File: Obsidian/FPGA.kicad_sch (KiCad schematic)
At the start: 45 parts, among them Q1 BSS138LT1G, Q2 BSS138LT1G, SW2 SW_DIP_x01, U1 XC7A35T-CSG325, U28 24AA256UID-I_ST

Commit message: update LCSC reference, and OFFSET rotation for JLCPCB
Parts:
- LD3, LD4: LCSC C5879295 -> C598257
- U28: FT Rotation Offset (none) -> 270
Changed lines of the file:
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@@
 			)
 		)
-		(property "LCSC" "C5879295"
+		(property "LCSC" "C598257"
 			(at 179.07 240.03 90)
 			(effects
@@
 			)
 		)
-		(property "FT Rotation Offset" ""
+		(property "FT Rotation Offset" "270"
 			(at 106.68 232.41 0)
 			(effects
@@
 			)
 		)
-		(property "LCSC" "C5879295"
+		(property "LCSC" "C598257"
 			(at 214.63 240.03 90)
 			(effects

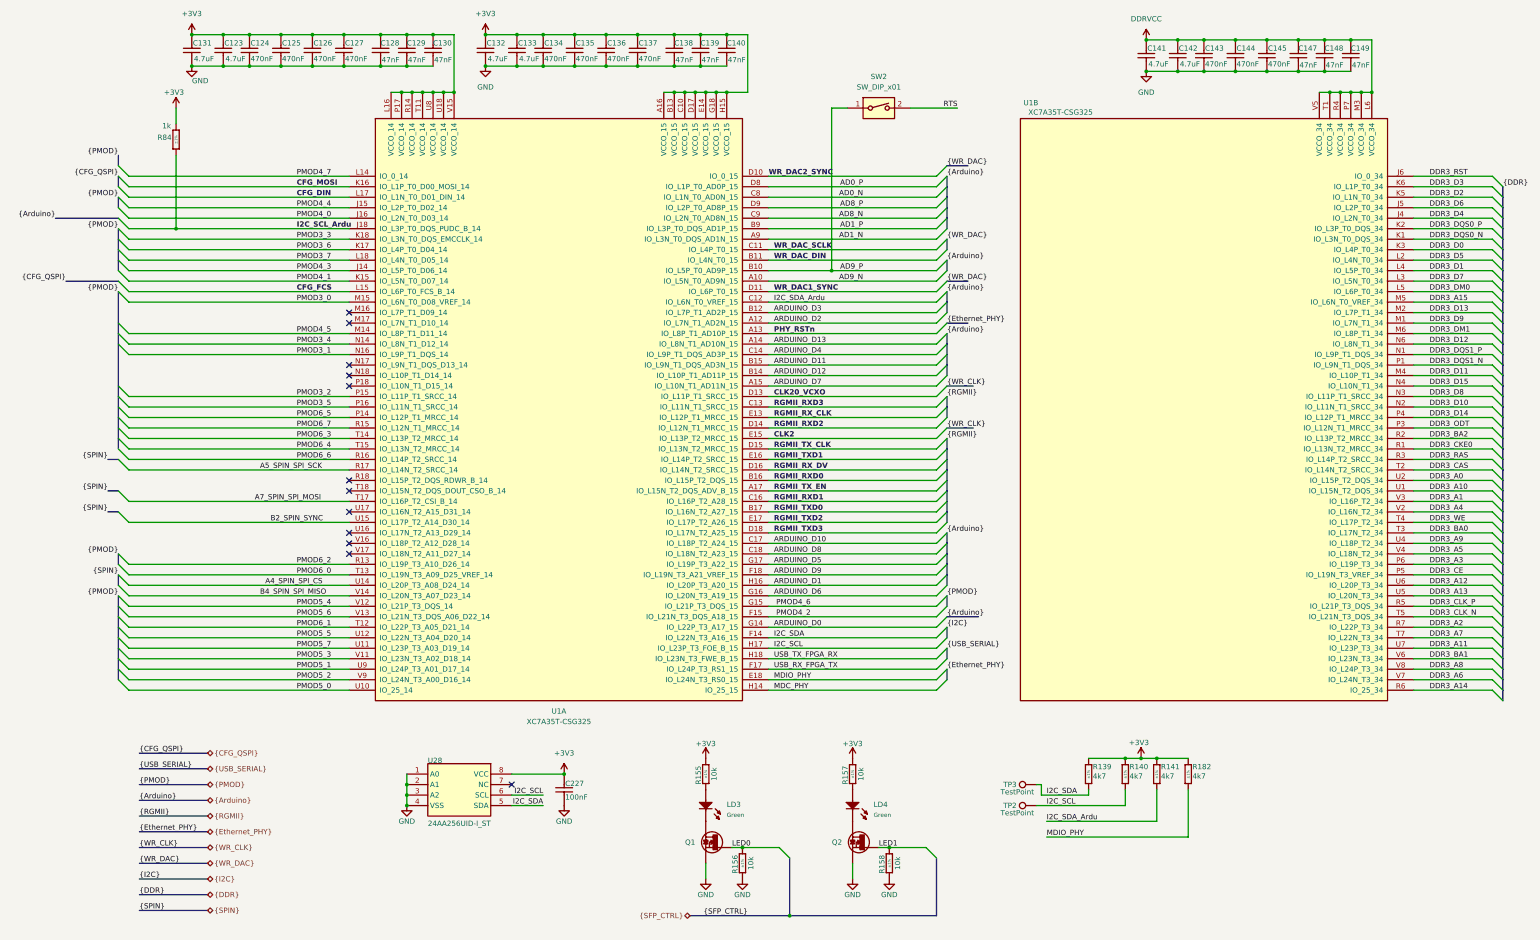
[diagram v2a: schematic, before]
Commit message: Cleaning symbol fields
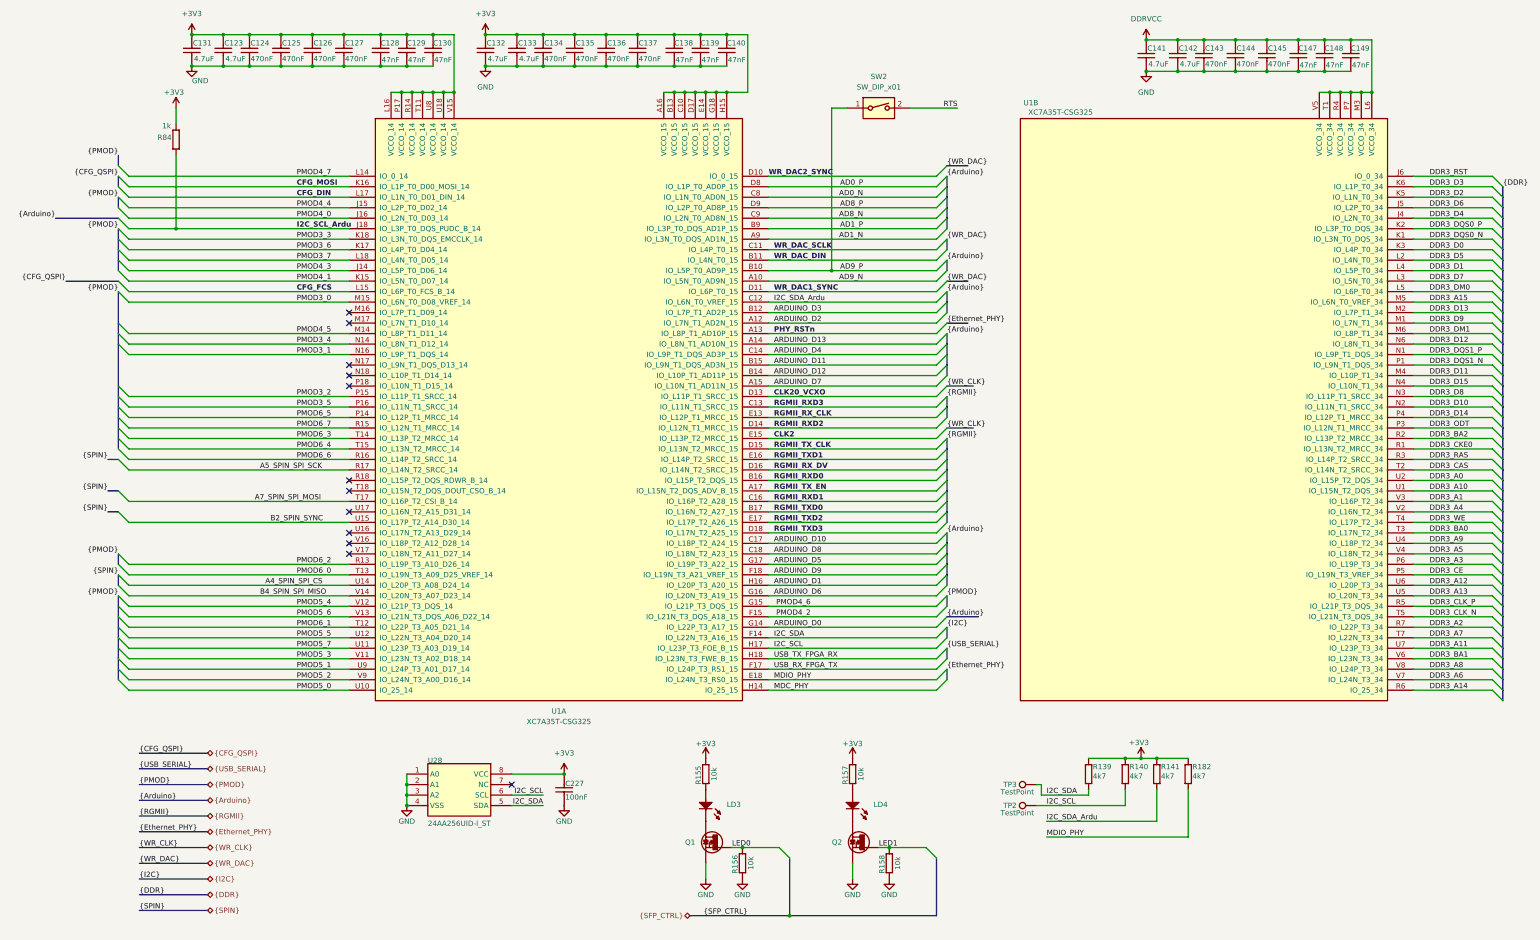
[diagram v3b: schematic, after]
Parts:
- C123, C131, C132, C133, C141, C142: Author CERN DEM BC -> (none); Case 0402 -> (none); Comment 4.7uF -> (none); Component Kind Standard -> (none); Component Type Standard -> (none); ComponentHeight (none) -> (none); CreateDate 09/07/20 00:00:00 -> (none); Database Table Name Capacitors -> (none); Footprint Library Capacitors SMD -> (none); Footprint Path PcbLib\Capacitors SMD.PcbLib -> (none); Footprint Ref CAPC1005X55N -> (none); HelpURL \\cern.ch\dfs\Applications\Altium\Datasheets\CC0402_X5R_YAG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 -> (none); LatestRevisionDate 09/07/20 00:00:00 -> (none); Library Name Capacitors SMD -> (none); Library Path SchLib\Capacitors.SchLib -> (none); Library Ref Capacitor - non polarized -> (none); License CC-BY-SA 4.0 -> (none); Manufacturer GENERIC -> (none); Manufacturer Part Number CC0402_4.7UF_16V_20%_X5R -> (none); Manufacturer1 ComponentHeight 0.55mm -> (none); Manufacturer1 Example YAGEO PHYCOMP -> (none); Manufacturer1 Part Number CC0402MRX5R7BB475 -> (none); Mounted Yes -> (none); PackageDescription (none) -> (none); Part Description SMD Multilayer Chip Ceramic Capacitor -> (none); Part Number CC0402_4.7UF_16V_20%_X5R -> (none); Pin Count 2 -> (none); PressFit (none) -> (none); SMD Yes -> (none); Sense No -> (none); Sense Comment (none) -> (none); Socket No -> (none); Status Preferred -> (none); Status Comment (none) -> (none); TC X5R -> (none); Tolerance ±20% -> (none); Voltage 16V -> (none)
- C124, C125, C126, C127, C134, C135, C136, C137, C143, C144, C145: Author CERN DEM JLC -> (none); Case 0201 -> (none); Comment 470nF -> (none); Component Kind Standard -> (none); Component Type Standard -> (none); ComponentHeight (none) -> (none); CreateDate 05/27/10 00:00:00 -> (none); Database Table Name Capacitors -> (none); Footprint Library Capacitors SMD -> (none); Footprint Path PcbLib\Capacitors SMD.PcbLib -> (none); Footprint Ref CAPC0603X33N -> (none); HelpURL \\cern.ch\dfs\Applications\Altium\Datasheets\CC0201_X5R_TAI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 -> (none); LatestRevisionDate 05/27/10 00:00:00 -> (none); Library Name Capacitors SMD -> (none); Library Path SchLib\Capacitors.SchLib -> (none); Library Ref Capacitor - non polarized -> (none); License CC-BY-SA 4.0 -> (none); Manufacturer GENERIC -> (none); Manufacturer Part Number CC0201_470NF_4V_20%_X5R -> (none); Manufacturer1 ComponentHeight 0.33mm -> (none); Manufacturer1 Example TAIYO YUDEN -> (none); Manufacturer1 Part Number AMK063BJ474MP-F -> (none); Mounted Yes -> (none); PackageDescription (none) -> (none); Part Description SMD Multilayer Chip Ceramic Capacitor -> (none); Part Number CC0201_470NF_4V_20%_X5R -> (none); Pin Count 2 -> (none); PressFit (none) -> (none); SMD Yes -> (none); Sense No -> (none); Sense Comment (none) -> (none); Socket No -> (none); Status Not Recommended -> (none); Status Comment (none) -> (none); TC X5R -> (none); Tolerance ±20% -> (none); Voltage 4V -> (none)
- C128, C129, C130, C138, C139, C140, C147, C148, C149: Author CERN DEM JLC -> (none); Case 0201 -> (none); Comment 47nF -> (none); Component Kind Standard -> (none); Component Type Standard -> (none); ComponentHeight (none) -> (none); CreateDate 12/03/07 00:00:00 -> (none); Database Table Name Capacitors -> (none); Footprint Library Capacitors SMD -> (none); Footprint Path PcbLib\Capacitors SMD.PcbLib -> (none); Footprint Ref CAPC0603X33N -> (none); HelpURL \\cern.ch\dfs\Applications\Altium\Datasheets\CC0201_X5R_AVX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 -> (none); LatestRevisionDate 12/03/07 00:00:00 -> (none); Library Name Capacitors SMD -> (none); Library Path SchLib\Capacitors.SchLib -> (none); Library Ref Capacitor - non polarized -> (none); License CC-BY-SA 4.0 -> (none); Manufacturer GENERIC -> (none); Manufacturer Part Number CC0201_47NF_6.3V_10%_X5R -> (none); Manufacturer1 ComponentHeight 0.33mm -> (none); Manufacturer1 Example AVX -> (none); Manufacturer1 Part Number 02016D473KAT2A -> (none); Mounted Yes -> (none); PackageDescription (none) -> (none); Part Description SMD Multilayer Chip Ceramic Capacitor -> (none); Part Number CC0201_47NF_6.3V_10%_X5R -> (none); Pin Count 2 -> (none); PressFit (none) -> (none); SMD Yes -> (none); Sense No -> (none); Sense Comment (none) -> (none); Socket No -> (none); Status Not Recommended -> (none); Status Comment (none) -> (none); TC X5R -> (none); Tolerance ±10% -> (none); Voltage 6.3V -> (none)
- C227: Author CERN DEM MR -> (none); Case 0402 -> (none); Comment 100nF -> (none); Component Kind Standard -> (none); Component Type Standard -> (none); ComponentHeight (none) -> (none); CreateDate 06/30/17 00:00:00 -> (none); Database Table Name Capacitors -> (none); Footprint Library Capacitors SMD -> (none); Footprint Path PcbLib\Capacitors SMD.PcbLib -> (none); Footprint Ref CAPC1005X55N -> (none); HelpURL \\cern.ch\dfs\Applications\Altium\Datasheets\CC0402_MURATA_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 -> (none); LatestRevisionDate 06/30/17 00:00:00 -> (none); Library Name Capacitors SMD -> (none); Library Path SchLib\Capacitors.SchLib -> (none); Library Ref Capacitor - non polarized -> (none); License CC-BY-SA 4.0 -> (none); Manufacturer GENERIC -> (none); Manufacturer Part Number CC0402_100NF_50V_10%_X7R -> (none); Manufacturer1 ComponentHeight 0.55mm -> (none); Manufacturer1 Example MURATA -> (none); Manufacturer1 Part Number GRM155R71H104KE14D -> (none); Mounted Yes -> (none); PackageDescription (none) -> (none); Part Description SMD Multilayer Chip Ceramic Capacitor -> (none); Part Number CC0402_100NF_50V_10%_X7R -> (none); Pin Count 2 -> (none); PressFit (none) -> (none); SMD Yes -> (none); Sense No -> (none); Sense Comment (none) -> (none); Socket No -> (none); Status None -> (none); Status Comment (none) -> (none); TC X7R -> (none); Tolerance ±10% -> (none); Voltage 50V -> (none)
- LD3, LD4: Author CERN DEM JLC -> (none); Bonding No -> (none); Case 0603 -> (none); Color Green -> (none); Comment (none) -> (none); Component Kind Standard -> (none); Component Type Standard -> (none); ComponentHeight 0.65mm -> (none); ComponentLink1Description (none) -> (none); ComponentLink1URL (none) -> (none); ComponentLink2Description (none) -> (none); ComponentLink2URL (none) -> (none); CreateDate 07/03/17 00:00:00 -> (none); Database Table Name ICs And Semiconductors -> (none); Device (none) -> (none); Footprint Library ICs And Semiconductors SMD -> (none); Footprint Path PcbLib\ICs And Semiconductors SMD.PcbLib -> (none); Footprint Ref LED_KINGBRIGHT_KPH-1608CGCK -> (none); HelpURL \\cern.ch\dfs\Applications\Altium\Datasheets\LED_KINGBRIGHT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 -> (none); LatestRevisionDate 07/03/17 00:00:00 -> (none); Library Name LEDs & Displays -> (none); Library Path SchLib\LEDs & Displays.SchLib -> (none); Library Ref LED Green 1C 2A -> (none); License CC-BY-SA 4.0 -> (none); Manufacturer KINGBRIGHT -> (none); Manufacturer Part Number KPH-1608CGCK -> (none); Mounted Yes -> (none); PackageDescription SMT Green LED, Case 0603, Body L 1.6 x W 0.8mm H 0.65mm -> (none); Part Description SMD Green LED, Case 1.6mmX0.8mm(0603), 0.65mm Thickness -> (none); Part Number LED_KINGBRIGHT_KPH-1608CGCK -> (none); Pin Count 2 -> (none); PressFit No -> (none); SMD Yes -> (none); Sense No -> (none); Sense Comment (none) -> (none); Socket No -> (none); Status (none) -> (none); Status Comment (none) -> (none)
- Q1, Q2: Author CERN DEM JLC -> (none); Bonding No -> (none); Case SOT23-3 -> (none); Comment BSS138LT1G -> (none); Component Kind Standard -> (none); Component Type Standard -> (none); ComponentHeight 1.11mm -> (none); ComponentLink1Description (none) -> (none); ComponentLink1URL (none) -> (none); ComponentLink2Description (none) -> (none); ComponentLink2URL (none) -> (none); CreateDate 03/23/09 00:00:00 -> (none); Database Table Name ICs And Semiconductors -> (none); Device BSS138LT1G -> (none); Footprint Library ICs And Semiconductors SMD -> (none); Footprint Path PcbLib\ICs And Semiconductors SMD.PcbLib -> (none); Footprint Ref SOT95P240X110-3N -> (none); HelpURL \\cern.ch\dfs\Applications\Altium\Datasheets\BSS138LT1G.pdf -> (none); LatestRevisionDate 05/25/22 00:00:00 -> (none); LatestRevisionDate1 (none) -> (none); Library Name Transistors -> (none); Library Path SchLib\Transistors.SchLib -> (none); Library Ref N-MOSFET-D 1G 2S 3D -> (none); License CC-BY-SA 4.0 -> (none); Manufacturer ON SEMICONDUCTOR -> (none); Manufacturer Part Number BSS138L -> (none); Mounted Yes -> (none); PackageDescription SOT23, 0.95mm Pitch; 3 Pin, 1.40mm W X 3.00mm L X 1.10mm H 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 -> (none); Part Description 50V, 200mA N-Channel Enhancement Mode Field-Effect Transist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 -> (none); Part Number BSS138LT1G -> (none); Pin Count 3 -> (none); PressFit No -> (none); SCEM (none) -> (none); SMD Yes -> (none); Sense No -> (none); Sense Comment (none) -> (none); Socket No -> (none); Status (none) -> (none); Status Comment (none) -> (none)
- R139, R140, R141, R182: Author CERN DEM JLC -> (none); Case 0402 -> (none); Comment 4k7 -> (none); Component Kind Standard -> (none); Component Type Standard -> (none); ComponentHeight (none) -> (none); CreateDate 12/03/07 00:00:00 -> (none); Database Table Name Resistors -> (none); Footprint Library Resistors SMD -> (none); Footprint Path PcbLib\Resistors SMD.PcbLib -> (none); Footprint Ref RESC1005X40N -> (none); HelpURL \\cern.ch\dfs\Applications\Altium\Datasheets\R0402_Phycomp_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 -> (none); LatestRevisionDate 10/17/12 00:00:00 -> (none); Library Name Resistors SMD -> (none); Library Path SchLib\Resistors.SchLib -> (none); Library Ref Resistor - 1% -> (none); License CC-BY-SA 4.0 -> (none); Manufacturer GENERIC -> (none); Manufacturer Part Number R0402_4K7_1%_0.0625W_100PPM -> (none); Manufacturer1 ComponentHeight 0.4mm -> (none); Manufacturer1 Example YAGEO PHYCOMP -> (none); Manufacturer1 Part Number 232270674702L -> (none); Mounted Yes -> (none); PackageDescription (none) -> (none); Part Description General Purpose Thick Film Chip Resistor -> (none); Part Number R0402_4K7_1%_0.0625W_100PPM -> (none); Pin Count 2 -> (none); Power 0.0625W -> (none); PressFit No -> (none); SMD Yes -> (none); Sense No -> (none); Sense Comment (none) -> (none); Socket No -> (none); Status Not Recommended -> (none); Status Comment (none) -> (none); TC ±100ppm/°C -> (none); Tolerance ±1% -> (none); Voltage (none) -> (none)
- R155, R156, R157, R158: Author CERN DEM JLC -> (none); Case 0402 -> (none); Comment 10k -> (none); Component Kind Standard -> (none); Component Type Standard -> (none); ComponentHeight (none) -> (none); CreateDate 12/03/07 00:00:00 -> (none); Database Table Name Resistors -> (none); Footprint Library Resistors SMD -> (none); Footprint Path PcbLib\Resistors SMD.PcbLib -> (none); Footprint Ref RESC1005X40N -> (none); HelpURL \\cern.ch\dfs\Applications\Altium\Datasheets\R0402_Phycomp_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 -> (none); LatestRevisionDate 10/17/12 00:00:00 -> (none); Library Name Resistors SMD -> (none); Library Path SchLib\Resistors.SchLib -> (none); Library Ref Resistor - 1% -> (none); License CC-BY-SA 4.0 -> (none); Manufacturer GENERIC -> (none); Manufacturer Part Number R0402_10K_1%_0.0625W_100PPM -> (none); Manufacturer1 ComponentHeight 0.4mm -> (none); Manufacturer1 Example YAGEO PHYCOMP -> (none); Manufacturer1 Part Number 232270671003L -> (none); Mounted Yes -> (none); PackageDescription (none) -> (none); Part Description General Purpose Thick Film Chip Resistor -> (none); Part Number R0402_10K_1%_0.0625W_100PPM -> (none); Pin Count 2 -> (none); Power 0.0625W -> (none); PressFit No -> (none); SMD Yes -> (none); Sense No -> (none); Sense Comment (none) -> (none); Socket No -> (none); Status Not Recommended -> (none); Status Comment (none) -> (none); TC ±100ppm/°C -> (none); Tolerance ±1% -> (none); Voltage (none) -> (none)
- R84: Author CERN DEM JLC -> (none); Case 0402 -> (none); Comment 1k -> (none); Component Kind Standard -> (none); Component Type Standard -> (none); ComponentHeight (none) -> (none); CreateDate 12/03/07 00:00:00 -> (none); Database Table Name Resistors -> (none); Footprint Library Resistors SMD -> (none); Footprint Path PcbLib\Resistors SMD.PcbLib -> (none); Footprint Ref RESC1005X40N -> (none); HelpURL \\cern.ch\dfs\Applications\Altium\Datasheets\R0402_Phycomp_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 -> (none); LatestRevisionDate 10/17/12 00:00:00 -> (none); Library Name Resistors SMD -> (none); Library Path SchLib\Resistors.SchLib -> (none); Library Ref Resistor - 1% -> (none); License CC-BY-SA 4.0 -> (none); Manufacturer GENERIC -> (none); Manufacturer Part Number R0402_1K_1%_0.0625W_100PPM -> (none); Manufacturer1 ComponentHeight 0.4mm -> (none); Manufacturer1 Example YAGEO PHYCOMP -> (none); Manufacturer1 Part Number 232270671002L -> (none); Mounted Yes -> (none); PackageDescription (none) -> (none); Part Description General Purpose Thick Film Chip Resistor -> (none); Part Number R0402_1K_1%_0.0625W_100PPM -> (none); Pin Count 2 -> (none); Power 0.0625W -> (none); PressFit No -> (none); SMD Yes -> (none); Sense No -> (none); Sense Comment (none) -> (none); Socket No -> (none); Status Not Recommended -> (none); Status Comment (none) -> (none); TC ±100ppm/°C -> (none); Tolerance ±1% -> (none); Voltage (none) -> (none)
- U28: ARROW PART NUMBER 24AA256UID-I/ST -> (none); ARROW PRICE/STOCK https://www.arrow.com/en/products/24aa256uid-ist/microchip-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 -> (none); DATASHEET LINK https://datasheet.datasheetarchive.com/originals/distributo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 -> (none); GEOMETRY.HEIGHT 1.2mm -> (none); MANUFACTURER_NAME Microchip -> (none); MANUFACTURER_PART_NUMBER 24AA256UID-I/ST -> (none); MOUSER PART NUMBER 579-24AA256UID-I/ST -> (none); MOUSER PRICE/STOCK https://www.mouser.co.uk/ProductDetail/Microchip-Technology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 -> (none)

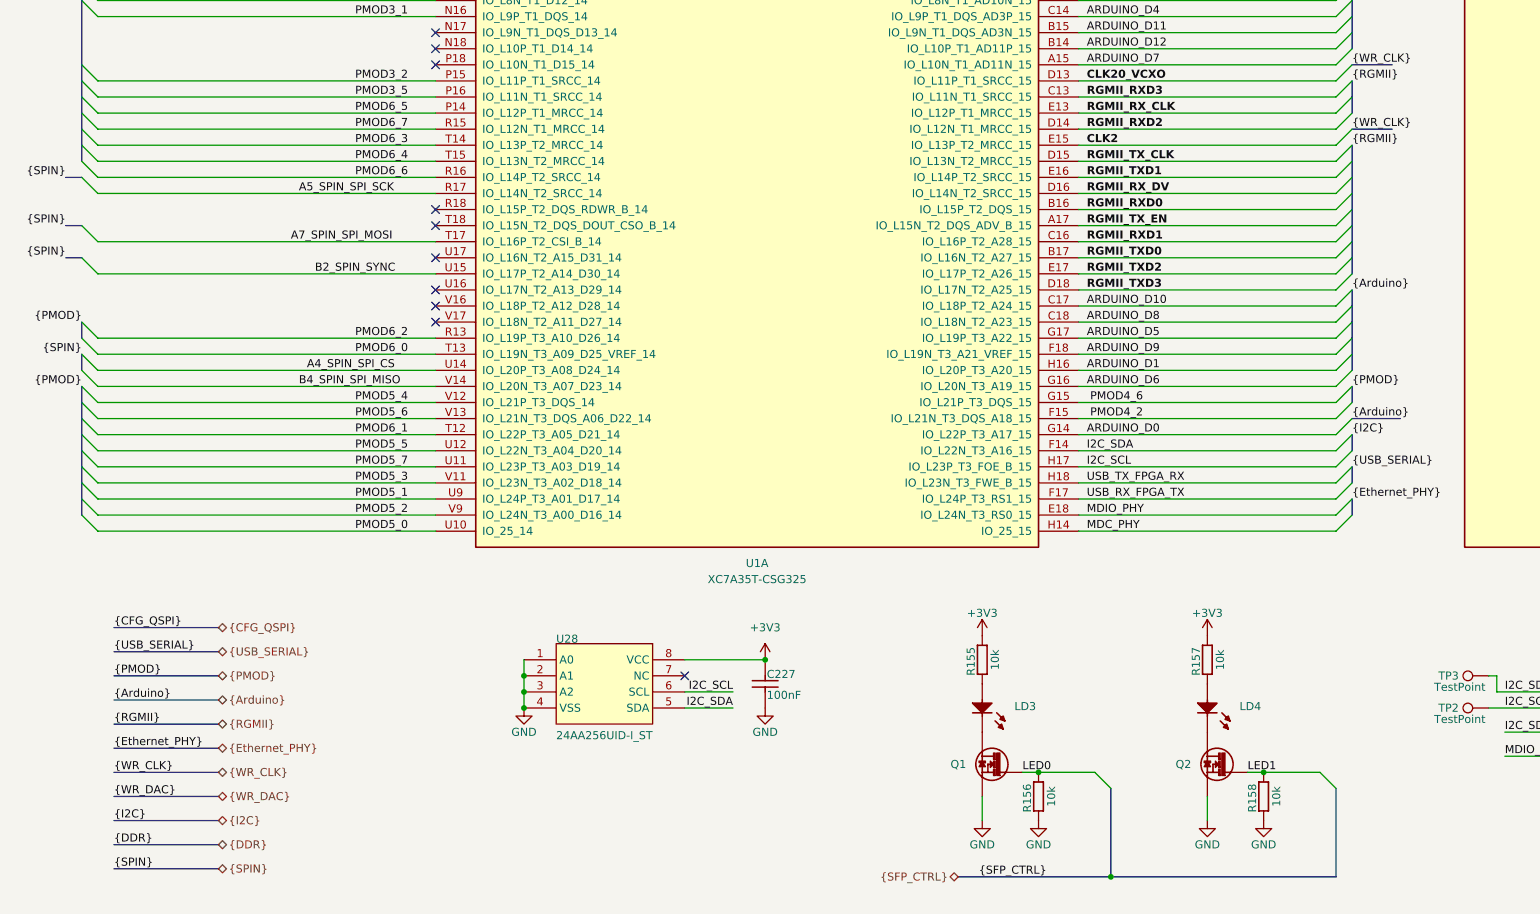
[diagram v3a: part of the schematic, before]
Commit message: Separating auxiliary clock from WR clock
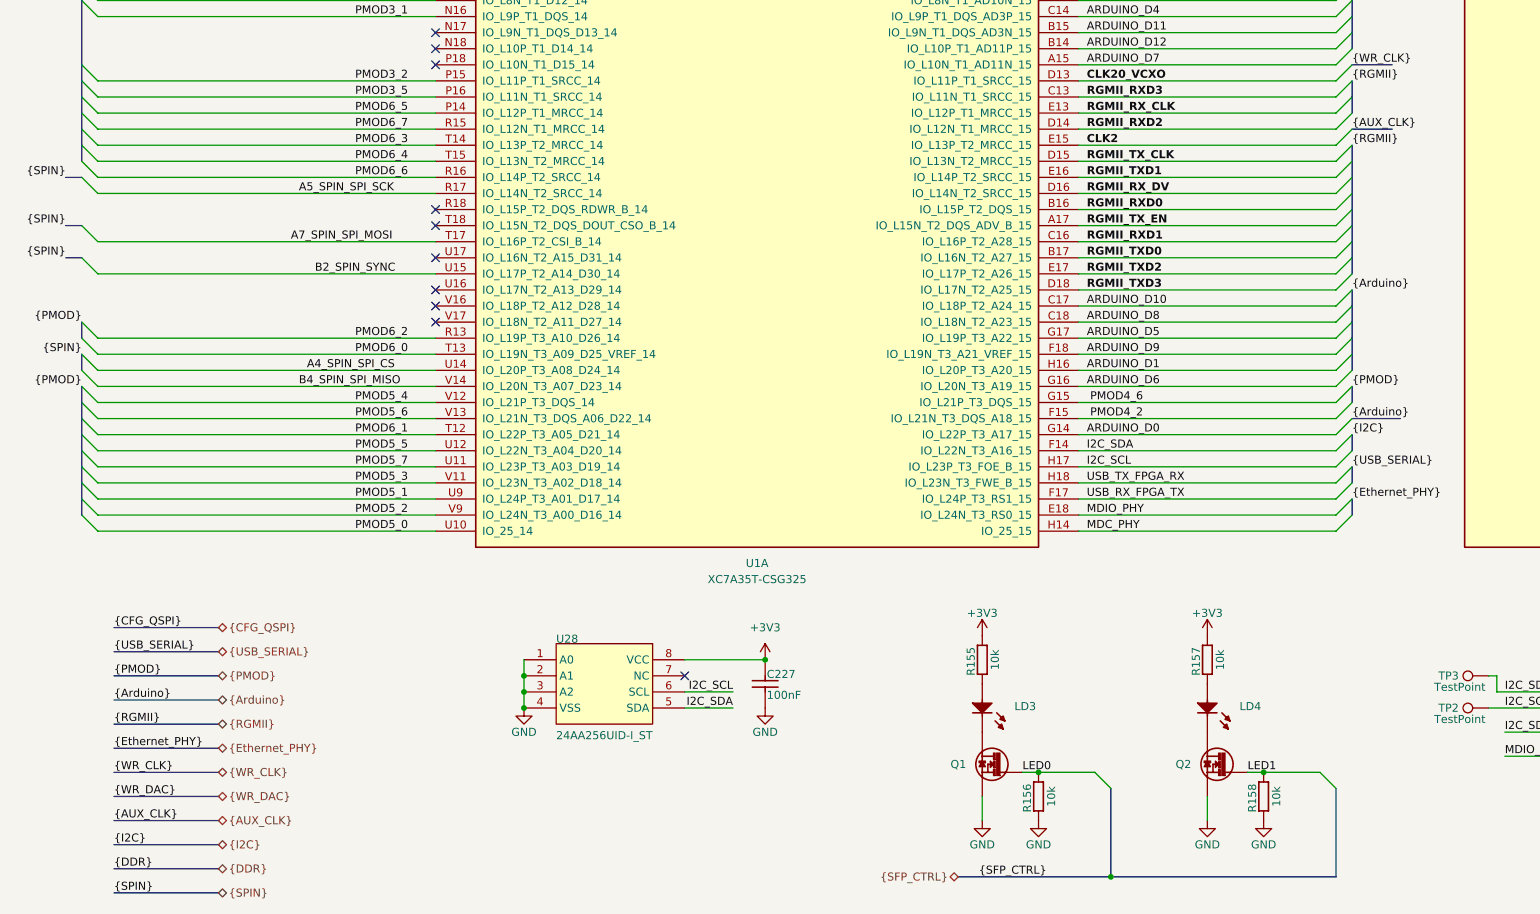
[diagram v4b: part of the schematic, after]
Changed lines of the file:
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@@
 	(bus
 		(pts
-			(xy 41.91 265.43) (xy 58.42 265.43)
+			(xy 41.91 269.24) (xy 58.42 269.24)
 		)
 		(stroke
@@
 		)
 	)
+	(bus
+		(pts
+			(xy 41.91 257.81) (xy 58.42 257.81)
+		)
+		(stroke
+			(width 0)
+			(type default)
+		)
+	)
 	(wire
 		(pts
@@
 	(bus
 		(pts
-			(xy 41.91 261.62) (xy 58.42 261.62)
+			(xy 41.91 265.43) (xy 58.42 265.43)
 		)
 		(stroke
@@
 	(bus
 		(pts
-			(xy 41.91 257.81) (xy 58.42 257.81)
+			(xy 41.91 261.62) (xy 58.42 261.62)
 		)
 		(stroke
@@
 	)
 	(label "{SPIN}"
-		(at 41.91 265.43 0)
+		(at 41.91 269.24 0)
 		(effects
 			(font
@@
 		)
 	)
+	(label "{AUX_CLK}"
+		(at 41.91 257.81 0)
+		(effects
+			(font
+				(size 1.27 1.27)
+			)
+			(justify left bottom)
+		)
+	)
 	(label "RGMII_TX_CLK"
 		(at 195.58 153.67 0)
@@
 	)
 	(label "{I2C}"
-		(at 41.91 257.81 0)
+		(at 41.91 261.62 0)
 		(effects
 			(font
@@
 	)
 	(label "{DDR}"
-		(at 41.91 261.62 0)
+		(at 41.91 265.43 0)
 		(effects
 			(font
@@
 		)
 	)
-	(label "{WR_CLK}"
+	(label "{AUX_CLK}"
 		(at 237.49 148.59 0)
 		(effects
@@
 		)
 	)
-	(hierarchical_label "{I2C}"
+	(hierarchical_label "{AUX_CLK}"
 		(shape bidirectional)
 		(at 58.42 257.81 0)
@@
 		)
 	)
+	(hierarchical_label "{I2C}"
+		(shape bidirectional)
+		(at 58.42 261.62 0)
+		(effects
+			(font
+				(size 1.27 1.27)
+			)
+			(justify left)
+		)
+	)
 	(hierarchical_label "{PMOD}"
 		(shape bidirectional)
@@
 	(hierarchical_label "{SPIN}"
 		(shape bidirectional)
-		(at 58.42 265.43 0)
+		(at 58.42 269.24 0)
 		(effects
 			(font
@@
 	(hierarchical_label "{DDR}"
 		(shape bidirectional)
-		(at 58.42 261.62 0)
+		(at 58.42 265.43 0)
 		(effects
 			(font

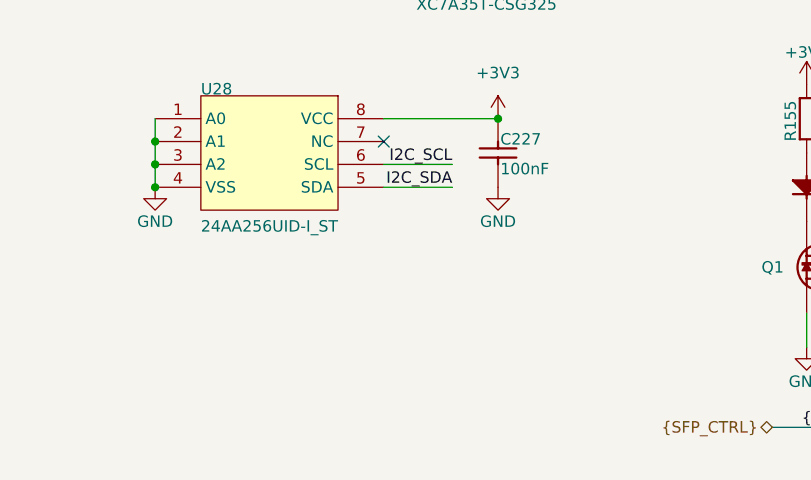
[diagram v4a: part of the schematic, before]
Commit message: adding resistor in SFP sheep for SFP/SFP+ compatibility
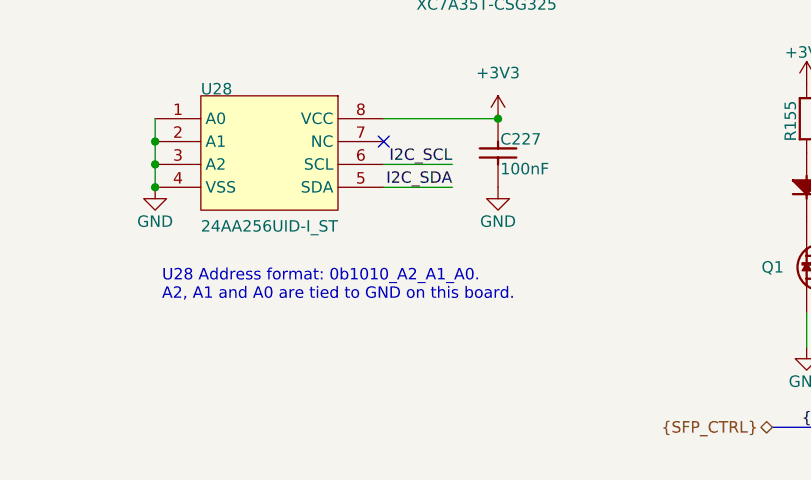
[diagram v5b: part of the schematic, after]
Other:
- note added: "U28 Address format: 0b1010_A2_A1_A0. A2, A1 and A0 are tied to GND on this board."
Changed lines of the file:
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@@
 		(members "WR_DAC2_SYNC" "WR_DAC_SCLK" "WR_DAC_DIN" "WR_DAC1_SYNC")
+	)
+	(text "U28 Address format: 0b1010_A2_A1_A0.\nA2, A1 and A0 are tied to GND on this board."
+		(exclude_from_sim no)
+		(at 107.442 250.952 0)
+		(effects
+			(font
+				(size 1.27 1.27)
+			)
+			(justify left)
+		)
 	)
 	(junction
